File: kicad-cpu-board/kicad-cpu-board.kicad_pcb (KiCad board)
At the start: 2 copper layers, 78.5 x 69 mm, 56 parts, among them J101 ICSP Header, J102 Conn_01x10_Male, J103 Conn_01x15_Female, J104 Conn_02x05_Odd_Even, Q101 2N7000, Q102 2N7000, Q103 2N7000, Q104 2N7000, U101 L7805, U102 LP2950-3.3_TO92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

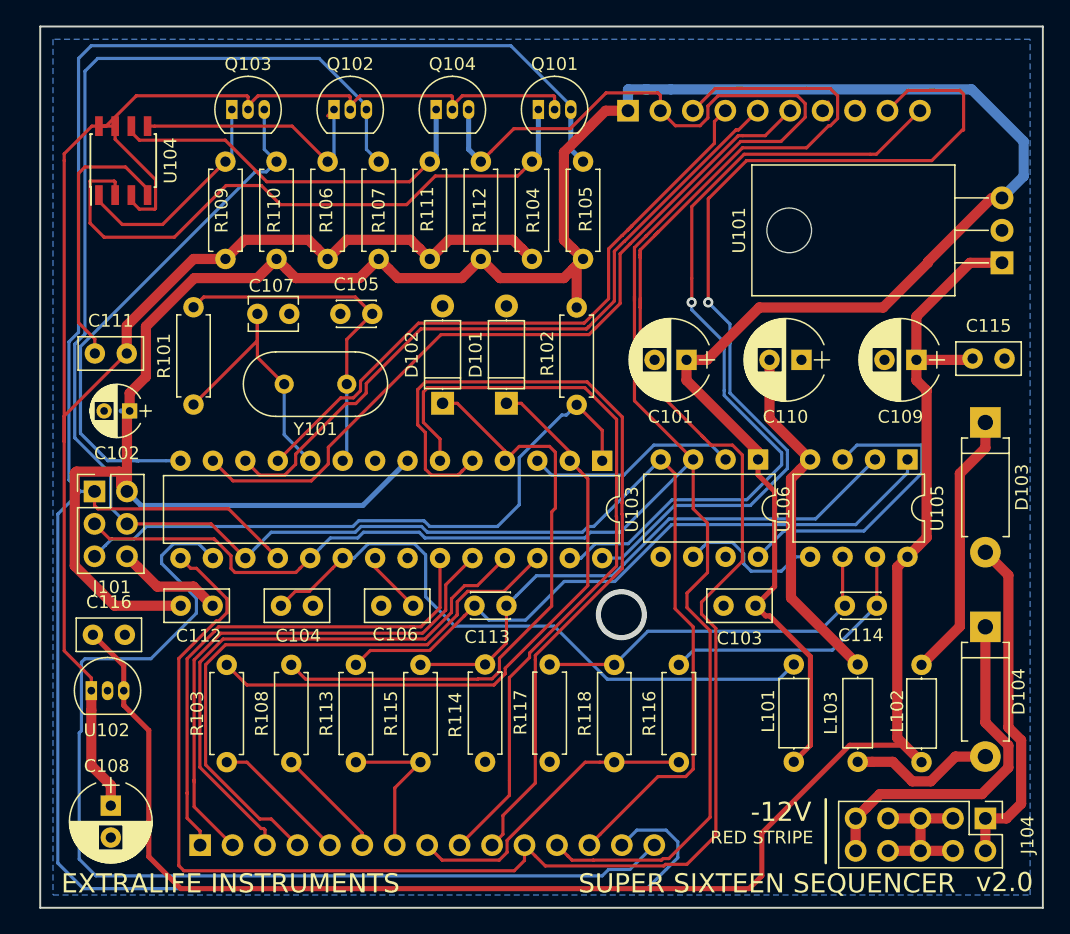
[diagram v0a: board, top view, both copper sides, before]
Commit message: Updating PCB and schematics for assembly bugfixes
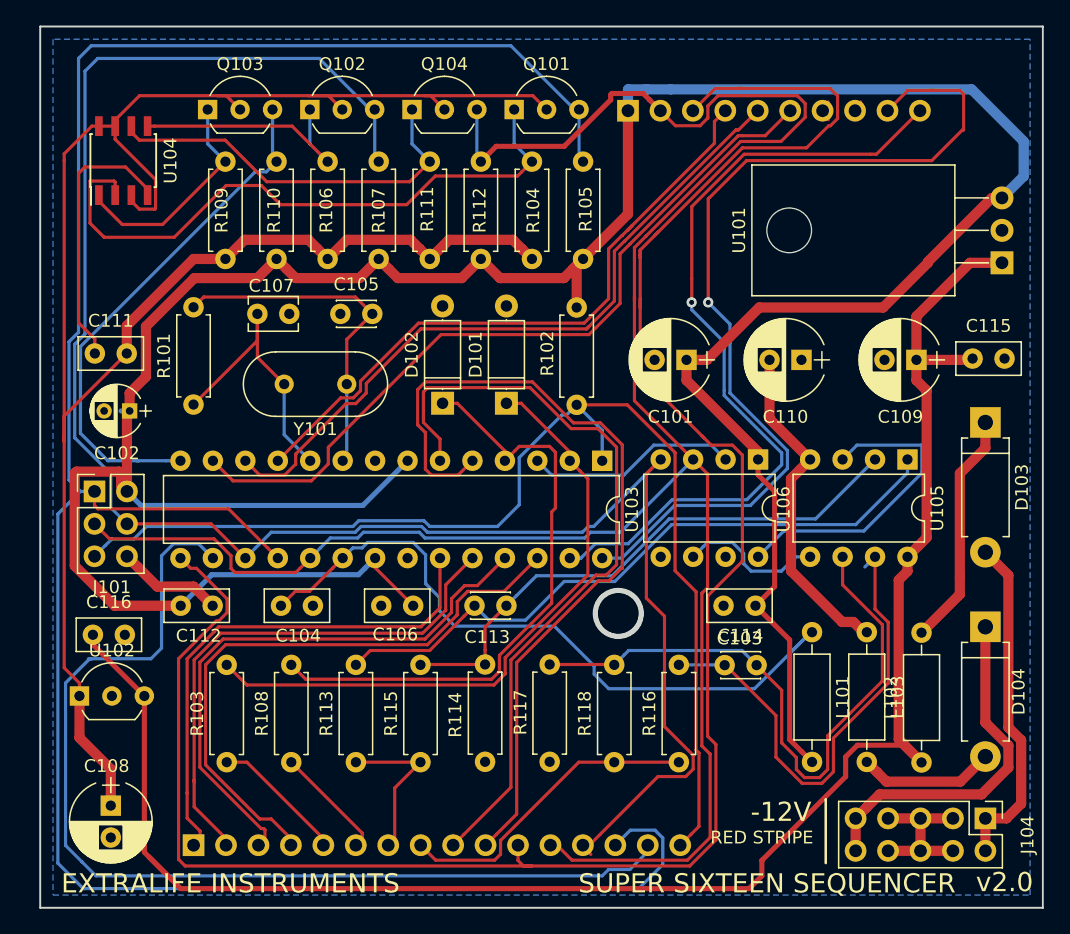
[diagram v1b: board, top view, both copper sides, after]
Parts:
- C109: value 47uF -> 330uf
- D101, D102: value 5.1v -> 1N4733A
- D104: value D -> 1N4001
- J103: value Conn_01x15_Female -> Conn_01x16_Female; footprint Pin_Headers:Pin_Header_Straight_1x15_Pitch2.54mm -> Pin_Headers:Pin_Header_Straight_1x16_Pitch2.54mm
- L101, L102, L103: value L -> 220uH; footprint Inductors_THT:L_Axial_L5.3mm_D2.2mm_P7.62mm_Horizontal_Vishay_IM-1 -> Inductors_THT:L_Axial_L6.6mm_D2.7mm_P10.16mm_Horizontal_Vishay_IM-2
- Q101, Q102, Q103, Q104, U102: footprint TO_SOT_Packages_THT:TO-92_Inline_Narrow_Oval -> TO_SOT_Packages_THT:TO-92_Inline_Wide
- R117: value 47k -> 10k
- moved C114 12.8 mm to (77.6, 93.0), turned to 0 degrees
- moved L101 2.90 mm to (84.4, 90.4)
- moved L103 2.63 mm to (88.7, 90.4)
- moved Q101 1.89 mm to (61.1, 49.5)
- moved Q102 1.89 mm to (45.1, 49.5)
- moved Q103 1.89 mm to (37.1, 49.5)
- moved Q104 1.89 mm to (53.1, 49.5)
- moved U102 1.02 mm to (27.1, 95.4)
- moved J103 0.51 mm to (36.0, 107.1)
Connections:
- C106 pad 1: Net-(C106-Pad1) -> +5V
- U103 pad 21: Net-(C106-Pad1) -> +5V
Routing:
- net RESET: track 50.4 -> 91.8 mm
- net Net-(C114-Pad2): track 28.9 -> 49.3 mm
- net +5V: track 225.6 -> 244.4 mm
- net Net-(C114-Pad1): track 21.3 -> 38.6 mm
- net Net-(C104-Pad1): track 49.0 -> 54.7 mm
- net Net-(C106-Pad1): track 4.96 -> 0.00 mm
- net +12V: track 136.9 -> 139.6 mm
- net Net-(D103-Pad1): track 21.1 -> 18.5 mm
- net MISO: track 185.2 -> 183.6 mm
- net CS0: track 83.1 -> 81.8 mm
- net SCK: track 170.0 -> 169.2 mm
- net Net-(D104-Pad2): track 11.4 -> 10.7 mm
- net MOSI: track 149.8 -> 150.5 mm
- net ResetIn: track 60.8 -> 60.1 mm
- net CV: track 24.2 -> 24.8 mm
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
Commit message: Adding R values to silkscreen
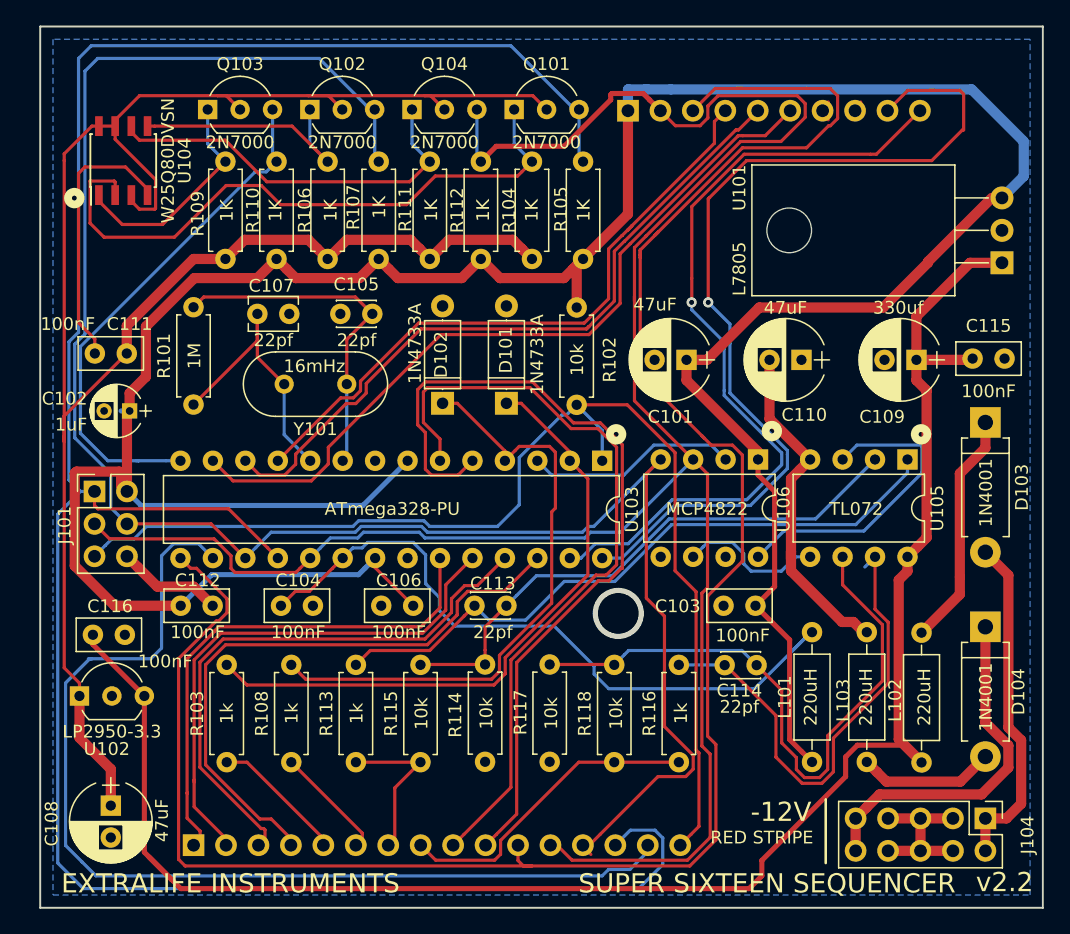
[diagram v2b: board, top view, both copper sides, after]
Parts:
- U102: value LP2950-3.3_TO92 -> LP2950-3.3
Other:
- board text added: "v2.2"
- board text removed: "v2.0"

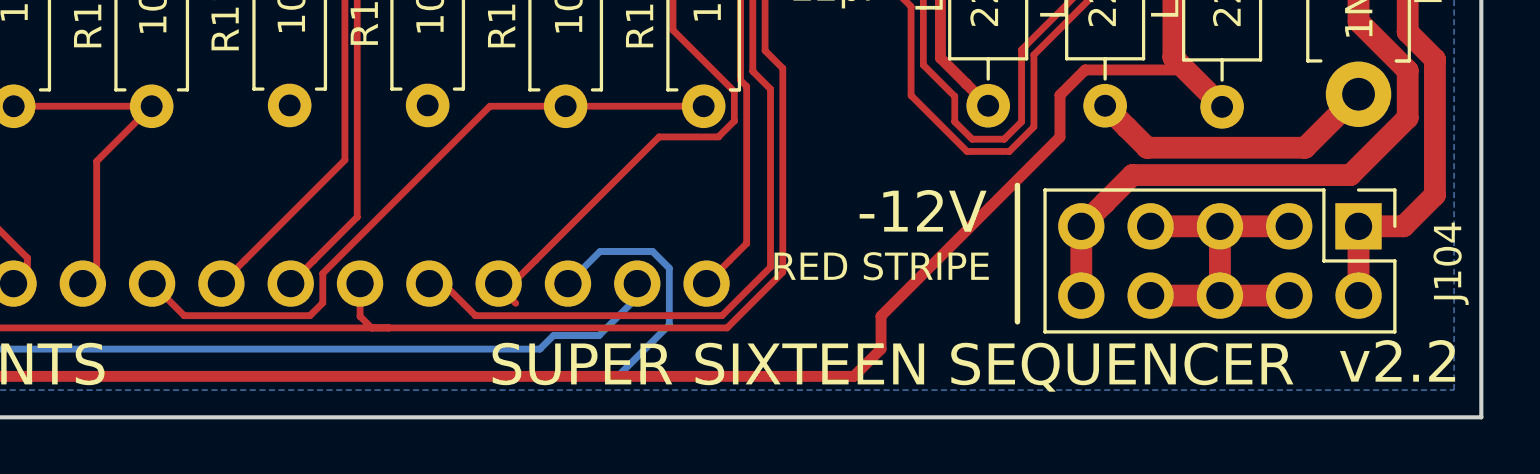
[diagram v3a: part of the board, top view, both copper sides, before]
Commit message: Updating CPU board version silkscreen
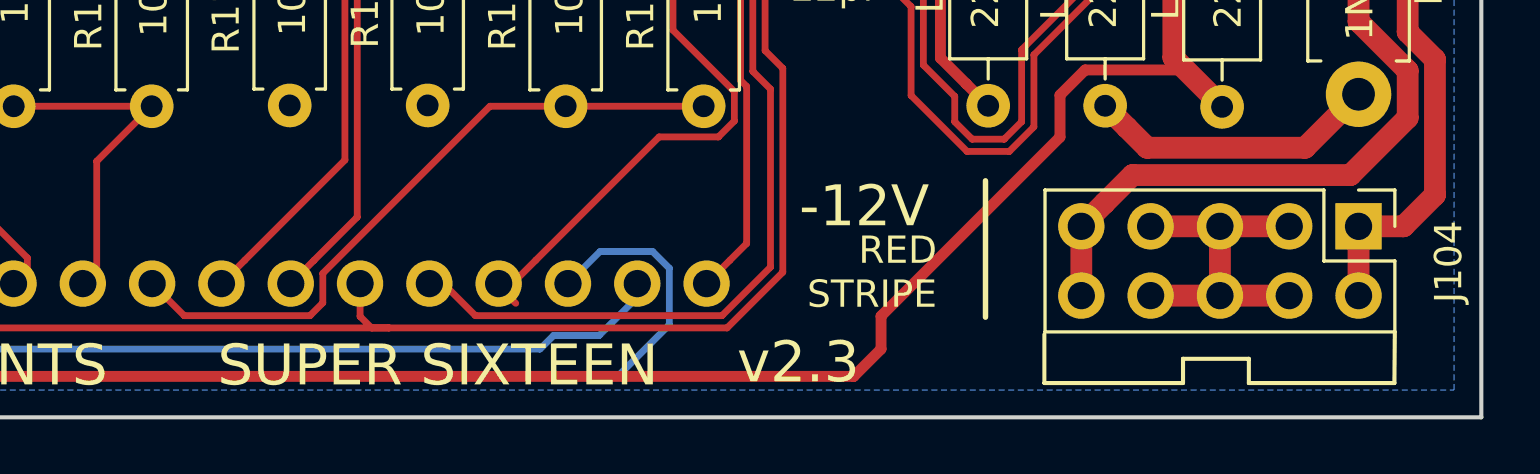
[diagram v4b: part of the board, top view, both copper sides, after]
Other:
- board text added: "SUPER SIXTEEN"
- board text added: "v2.3"
- board text removed: "SUPER SIXTEEN SEQUENCER"
- board text removed: "v2.2"
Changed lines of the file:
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@@
   (general
     (thickness 1.6)
-    (drawings 16)
+    (drawings 23)
     (tracks 786)
     (zones 0)
@@
     )
   )
+  (gr_line (start 86.487 108.966) (end 86.487 110.744) (layer F.SilkS) (width 0.15))
+  (gr_line (start 99.314 110.744) (end 99.33 108.87) (layer F.SilkS) (width 0.15))
+  (gr_line (start 93.98 110.744) (end 99.314 110.744) (layer F.SilkS) (width 0.15))
+  (gr_line (start 93.98 109.855) (end 93.98 110.744) (layer F.SilkS) (width 0.15))
+  (gr_line (start 91.567 109.855) (end 93.98 109.855) (layer F.SilkS) (width 0.15))
+  (gr_line (start 91.567 110.744) (end 91.567 109.855) (layer F.SilkS) (width 0.15))
+  (gr_line (start 86.487 110.744) (end 91.567 110.744) (layer F.SilkS) (width 0.15))
   (dimension 78.5 (width 0.3) (layer Eco1.User)
     (gr_text "78.500 mm" (at 63.25 37.9) (layer Eco1.User)
@@
     (arrow2b (pts (xy 24 40) (xy 25.126504 39.413579)))
   )
-  (gr_line (start 85.5 108.5) (end 85.5 103.5) (layer F.SilkS) (width 0.2))
+  (gr_line (start 84.328 108.331) (end 84.328 103.331) (layer F.SilkS) (width 0.2))
   (gr_circle (center 26.67 56.434) (end 26.97 56.434) (layer F.SilkS) (width 1))
   (gr_circle (center 92.964 74.93) (end 93.264 74.93) (layer F.SilkS) (width 1))
   (gr_circle (center 81.28 74.676) (end 81.58 74.676) (layer F.SilkS) (width 1))
   (gr_circle (center 69.088 74.93) (end 69.388 74.93) (layer F.SilkS) (width 1))
-  (gr_text "RED STRIPE" (at 80.5 106.5) (layer F.SilkS)
-    (effects (font (size 1 1) (thickness 0.2)))
+  (gr_text "RED\nSTRIPE" (at 82.55 106.68) (layer F.SilkS)
+    (effects (font (size 1 1) (thickness 0.2)) (justify right))
   )
-  (gr_text -12V (at 82 104.5) (layer F.SilkS)
+  (gr_text -12V (at 79.883 104.267) (layer F.SilkS)
     (effects (font (size 1.5 1.5) (thickness 0.3)))
   )
@@
     (effects (font (size 1.5 1.5) (thickness 0.3)))
   )
-  (gr_text "v2.2\n" (at 99.5 110) (layer F.SilkS)
+  (gr_text "v2.3\n" (at 77.47 109.982) (layer F.SilkS)
     (effects (font (size 1.5 1.5) (thickness 0.3)))
   )
-  (gr_text "SUPER SIXTEEN SEQUENCER" (at 80.9 110.1) (layer F.SilkS)
+  (gr_text "SUPER SIXTEEN" (at 64.262 110.1) (layer F.SilkS)
     (effects (font (size 1.5 1.5) (thickness 0.3)))
   )
